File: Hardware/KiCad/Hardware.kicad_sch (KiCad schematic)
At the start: 0 parts

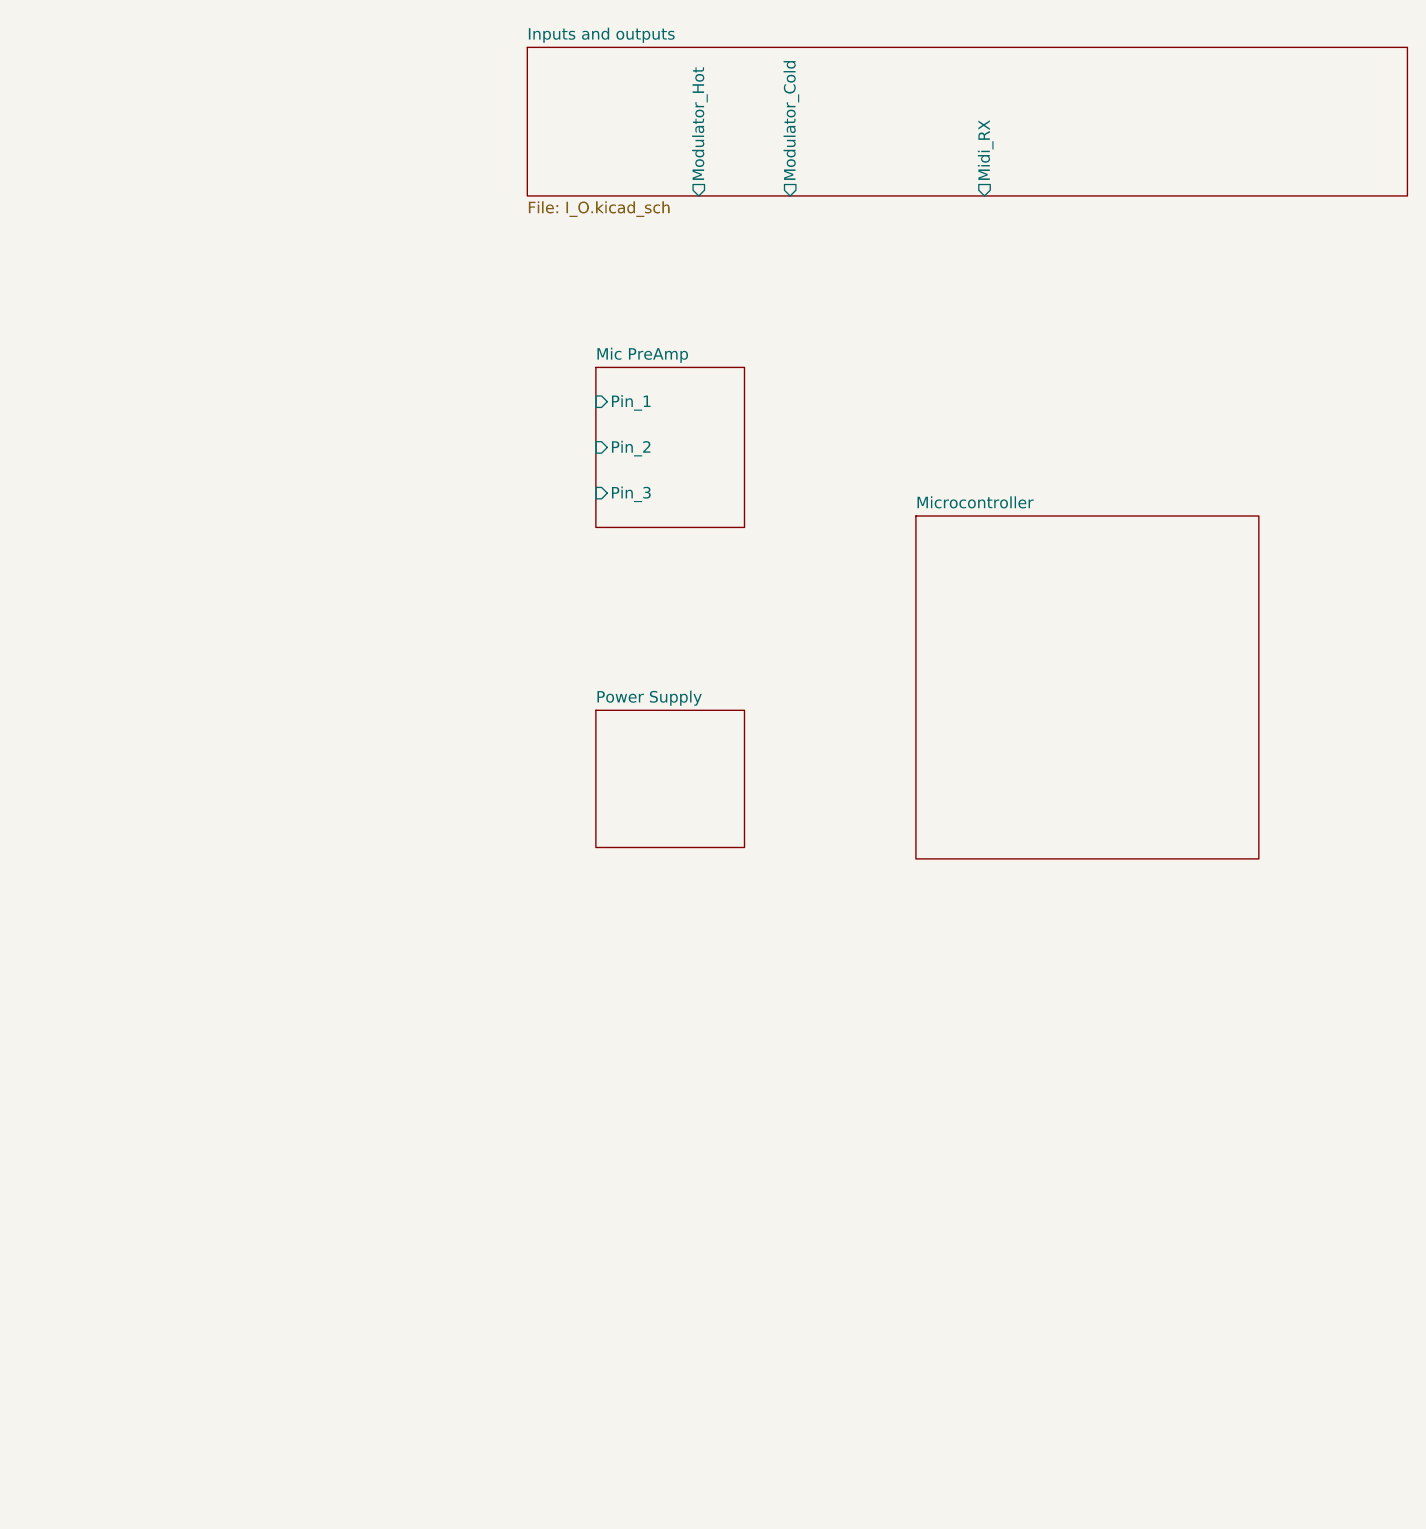
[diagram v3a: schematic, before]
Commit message: Re-orginanisation
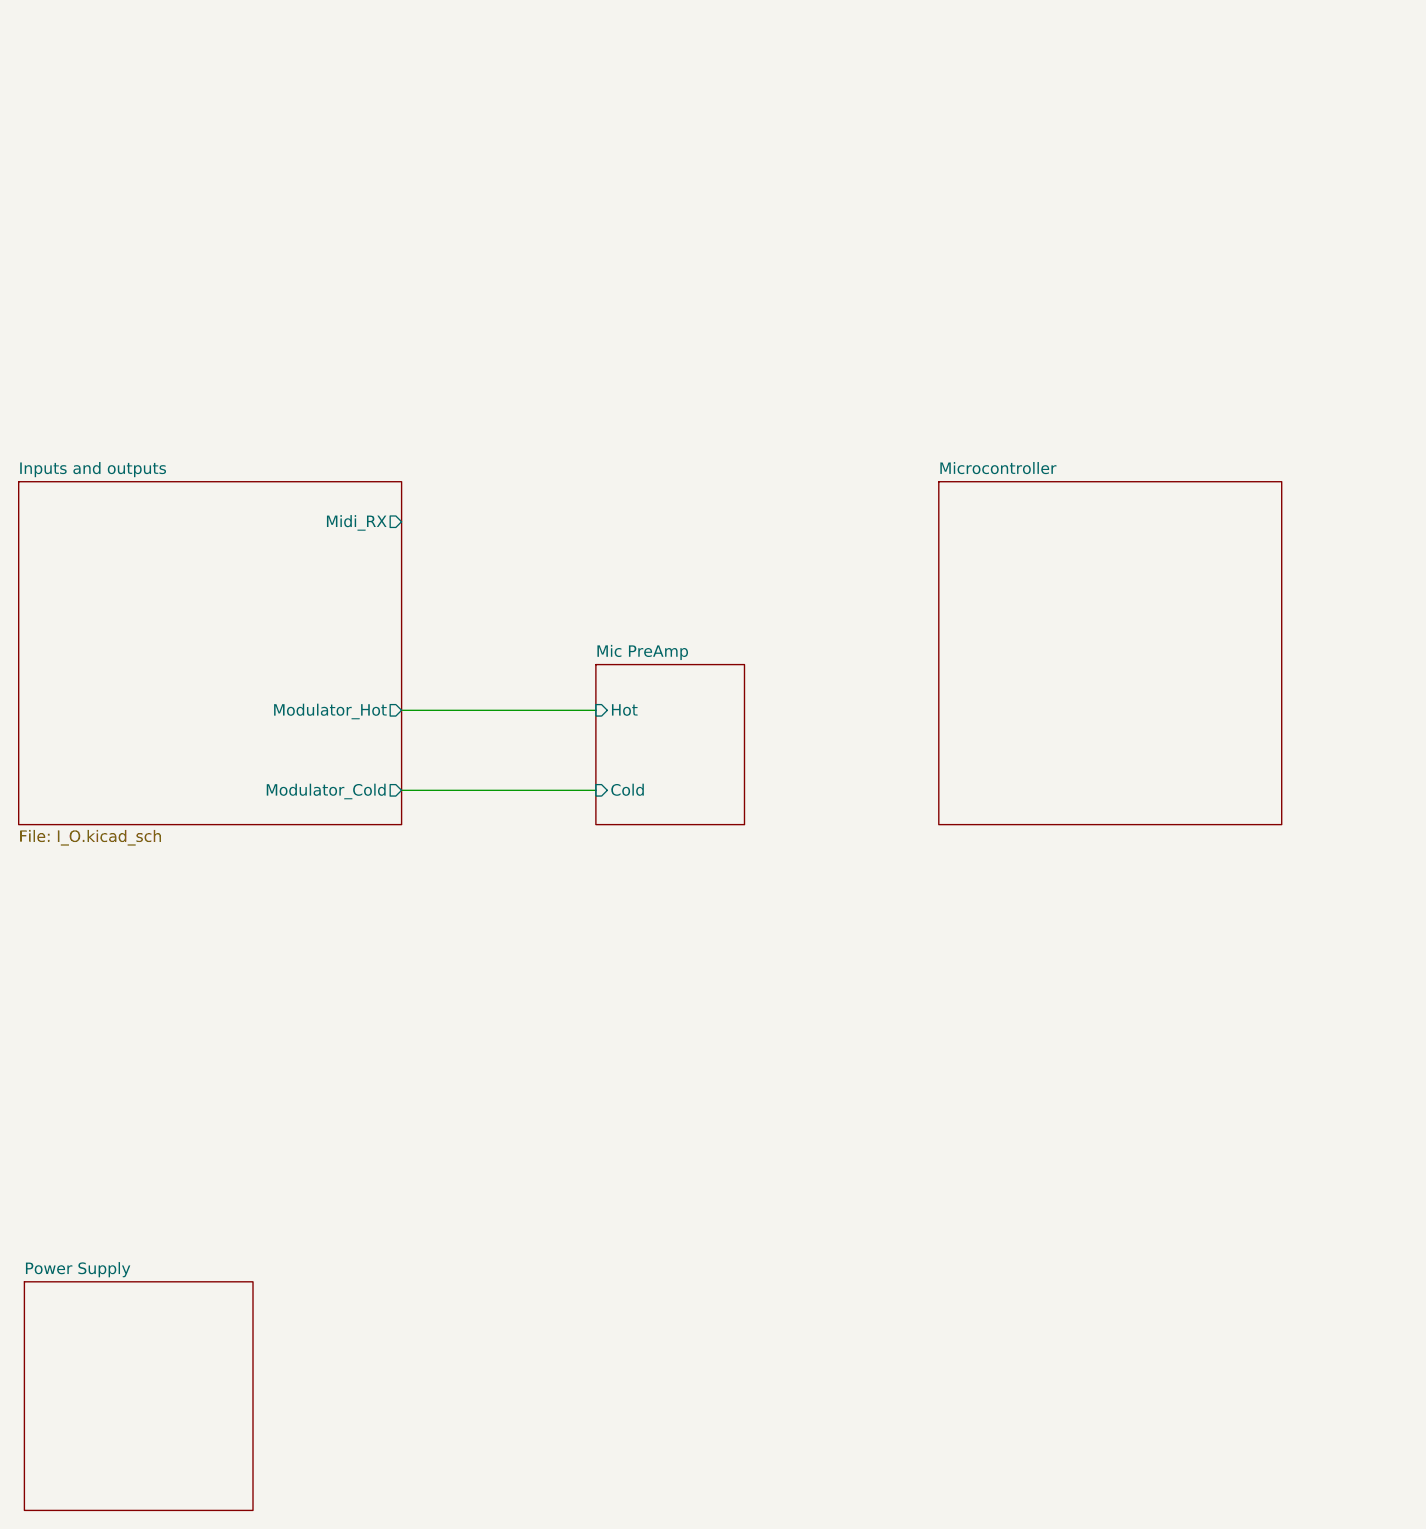
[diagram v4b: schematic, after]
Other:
- sheet Mic PreAmp ports: added Cold, Hot; removed Pin_1, Pin_2, Pin_3
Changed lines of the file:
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@@
 		(comment 1 "Tim Wannet")
 	)
-	(sheet
-		(at 124.46 80.01)
+	(wire
+		(pts
+			(xy 67.31 101.6) (xy 88.9 101.6)
+		)
+		(stroke
+			(width 0)
+			(type default)
+		)
+	)
+	(wire
+		(pts
+			(xy 67.31 110.49) (xy 88.9 110.49)
+		)
+		(stroke
+			(width 0)
+			(type default)
+		)
+	)
+	(sheet
+		(at 127 76.2)
 		(size 38.1 38.1)
 		(exclude_from_sim no)
@@
 		)
 		(property "Sheetname" "Microcontroller"
-			(at 124.46 79.2984 0)
+			(at 127 75.4884 0)
 			(effects
 				(font
@@
 		)
 		(property "Sheetfile" "MCU.kicad_sch"
-			(at 124.46 118.6946 0)
+			(at 127 114.8846 0)
 			(effects
 				(font
@@
 	)
 	(sheet
-		(at 81.28 27.94)
-		(size 97.79 16.51)
+		(at 24.765 76.2)
+		(size 42.545 38.1)
 		(exclude_from_sim no)
 		(in_bom yes)
@@
 		)
 		(property "Sheetname" "Inputs and outputs"
-			(at 81.28 27.2284 0)
+			(at 24.765 75.4884 0)
 			(effects
 				(font
@@
 		)
 		(property "Sheetfile" "I_O.kicad_sch"
-			(at 81.28 45.0346 0)
+			(at 24.765 114.8846 0)
 			(effects
 				(font
@@
 		)
 		(pin "Midi_RX" output
-			(at 132.08 44.45 270)
-			(effects
-				(font
-					(size 1.27 1.27)
-				)
-				(justify left)
+			(at 67.31 80.645 0)
+			(effects
+				(font
+					(size 1.27 1.27)
+				)
+				(justify right)
 			)
 		)
 		(pin "Modulator_Cold" output
-			(at 110.49 44.45 270)
-			(effects
-				(font
-					(size 1.27 1.27)
-				)
-				(justify left)
+			(at 67.31 110.49 0)
+			(effects
+				(font
+					(size 1.27 1.27)
+				)
+				(justify right)
 			)
 		)
 		(pin "Modulator_Hot" output
-			(at 100.33 44.45 270)
-			(effects
-				(font
-					(size 1.27 1.27)
-				)
-				(justify left)
+			(at 67.31 101.6 0)
+			(effects
+				(font
+					(size 1.27 1.27)
+				)
+				(justify right)
 			)
 		)
@@
 	)
 	(sheet
-		(at 88.9 101.6)
-		(size 16.51 15.24)
+		(at 25.4 165.1)
+		(size 25.4 25.4)
 		(exclude_from_sim no)
 		(in_bom yes)
@@
 		)
 		(property "Sheetname" "Power Supply"
-			(at 88.9 100.8884 0)
+			(at 25.4 164.3884 0)
 			(effects
 				(font
@@
 		)
 		(property "Sheetfile" "PSU.kicad_sch"
-			(at 88.9 117.4246 0)
+			(at 25.4 191.0846 0)
 			(effects
 				(font
@@
 	)
 	(sheet
-		(at 88.9 63.5)
+		(at 88.9 96.52)
 		(size 16.51 17.78)
 		(exclude_from_sim no)
@@
 		)
 		(property "Sheetname" "Mic PreAmp"
-			(at 88.9 62.7884 0)
+			(at 88.9 95.8084 0)
 			(effects
 				(font
@@
 		)
 		(property "Sheetfile" "PreAmp.kicad_sch"
-			(at 88.9 81.8646 0)
+			(at 88.9 114.8846 0)
 			(effects
 				(font
@@
 			)
 		)
-		(pin "Pin_1" input
-			(at 88.9 67.31 180)
+		(pin "Hot" input
+			(at 88.9 101.6 180)
 			(effects
 				(font
@@
 			)
 		)
-		(pin "Pin_2" input
-			(at 88.9 72.39 180)
-			(effects
-				(font
-					(size 1.27 1.27)
-				)
-				(justify left)
-			)
-		)
-		(pin "Pin_3" input
-			(at 88.9 77.47 180)
-			(effects
-				(font
+		(pin "Cold" input
+			(at 88.9 110.49 180)
+			(effects
+				(font
